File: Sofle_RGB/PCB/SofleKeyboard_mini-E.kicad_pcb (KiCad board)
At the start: 2 copper layers, 143.4 x 111.8 mm, 97 parts, among them J1 LED, J2 4PIN, J3 OLED, J4 key leds, J5 backlight sel, J6 indicator bypass, P1 i2c_pin, P2 i2c_pin, SW1 SW_PUSH-MX_W_LED, SW10 SW_PUSH-MX_W_LED, SW11 SW_PUSH-MX_W_LED, SW12 SW_PUSH-MX_W_LED, SW13 SW_PUSH-MX_W_LED, SW14 SW_PUSH-MX_W_LED, SW15 SW_PUSH-MX_W_LED, SW16 SW_PUSH-MX_W_LED, SW17 SW_PUSH-MX_W_LED, SW18 SW_PUSH-MX_W_LED, SW19 SW_PUSH-MX_W_LED, SW2 SW_PUSH-MX_W_LED, SW20 SW_PUSH-MX_W_LED, SW21 SW_PUSH-MX_W_LED, SW22 SW_PUSH-MX_W_LED, SW23 SW_PUSH-MX_W_LED, SW24 SW_PUSH-MX_W_LED, SW25 Rotary_Encoder_Switch, SW26 SW_PUSH-MX_W_LED, SW27 SW_PUSH-MX_W_LED, SW28 SW_PUSH-MX_W_LED, SW29 SW_PUSH-MX_W_LED, SW3 SW_PUSH-MX_W_LED, SW30 SW_PUSH-MX_W_LED, SW4 SW_PUSH-MX_W_LED, SW5 SW_PUSH-MX_W_LED, SW6 SW_PUSH-MX_W_LED, SW7 SW_PUSH-MX_W_LED, SW8 SW_PUSH-MX_W_LED, SW9 SW_PUSH-MX_W_LED, U1 ProMicro

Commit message: SK6812 mini-e RGB
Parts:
- D31, D32, D33, D34, D35, D36, D37: value LED_sk2812_SM -> LED-SK6812MINI-E; footprint LED_SMD:SK6812MINI_underglow_dev -> SofleRGB:SK6812MINI-E(mini_pinout)
- moved D34 7.95 mm to (106.7, 131.8), turned to 180 degrees
- moved D37 6.37 mm to (99.4, 86.5), turned to 90 degrees
- moved D33 5.57 mm to (196.6, 66.8)
- moved D35 5.45 mm to (149.0, 123.7), turned to 180 degrees
- moved D32 5.43 mm to (158.6, 59.2), turned to 180 degrees
- moved D31 4.91 mm to (120.5, 64.4)
- moved D36 4.16 mm to (187.3, 123.8), turned to 180 degrees
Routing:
- net Net-(SW22-Pad3): track 0.00 -> 74.4 mm, vias 0 -> 3
- net Net-(SW20-Pad3): track 1.18 -> 74.0 mm, vias 0 -> 6
- net Net-(SW24-Pad3): track 11.2 -> 82.2 mm, vias 1 -> 4
- net Net-(SW21-Pad1): track 0.00 -> 65.1 mm, vias 0 -> 2
- net Net-(SW23-Pad1): track 0.00 -> 47.8 mm, vias 0 -> 4
- net Net-(SW13-Pad3): track 0.00 -> 36.6 mm, vias 1 -> 3
- net Net-(SW11-Pad3): track 0.00 -> 35.1 mm, vias 0 -> 3
- net Net-(SW11-Pad1): track 0.00 -> 34.8 mm, vias 0 -> 3
- net Net-(SW13-Pad1): track 1.19 -> 35.8 mm, vias 0 -> 3
- net Net-(SW12-Pad1): track 0.00 -> 33.8 mm, vias 0 -> 2
- net Net-(SW12-Pad3): track 0.00 -> 33.3 mm, vias 0 -> 3
- net Net-(SW1-Pad1): track 0.00 -> 33.2 mm, vias 0 -> 2
- net Net-(SW3-Pad1): track 0.00 -> 32.3 mm, vias 0 -> 2
- net Net-(SW15-Pad1): track 0.00 -> 31.5 mm, vias 0 -> 3
- net Net-(SW2-Pad3): track 0.00 -> 31.1 mm, vias 0 -> 2
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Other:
- outline, holes or cut-outs redrawn

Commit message: Address PR comments + extra cleanup
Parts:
- SW1, SW10, SW11, SW12, SW13, SW14, SW15, SW16, SW17, SW18, SW19, SW2, SW20, SW21, SW22, SW23, SW24, SW26, SW27, SW28, SW29, SW3, SW30, SW4, SW5, SW6, SW7, SW8, SW9: footprint Dane:SK6812MINI-E_and_cherry(mini_pinout) -> SofleRGB:SK6812MINI-E_and_cherry(mini_pinout)
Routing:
- net GND: track 1077.0 -> 1079.7 mm, vias 246 -> 249
- net Net-(SW15-Pad1): track 31.5 -> 33.0 mm
- net Net-(SW14-Pad1): track 31.7 -> 30.4 mm
- net row3: track 190.7 -> 192.0 mm
- net Net-(SW21-Pad1): track 65.1 -> 64.0 mm
- net Net-(SW16-Pad3): track 30.7 -> 31.7 mm
- net Net-(SW22-Pad3): track 74.4 -> 73.4 mm
- net Net-(SW23-Pad1): track 47.8 -> 47.0 mm
- net Net-(SW14-Pad3): track 29.7 -> 28.9 mm
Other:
- board text added: "Sofle RGB v3.0, Dane Evans, Gustavo Baratto"
- board text removed: "&BL"
- board text removed: "Sofle RGB v2.0, Dane Evans"

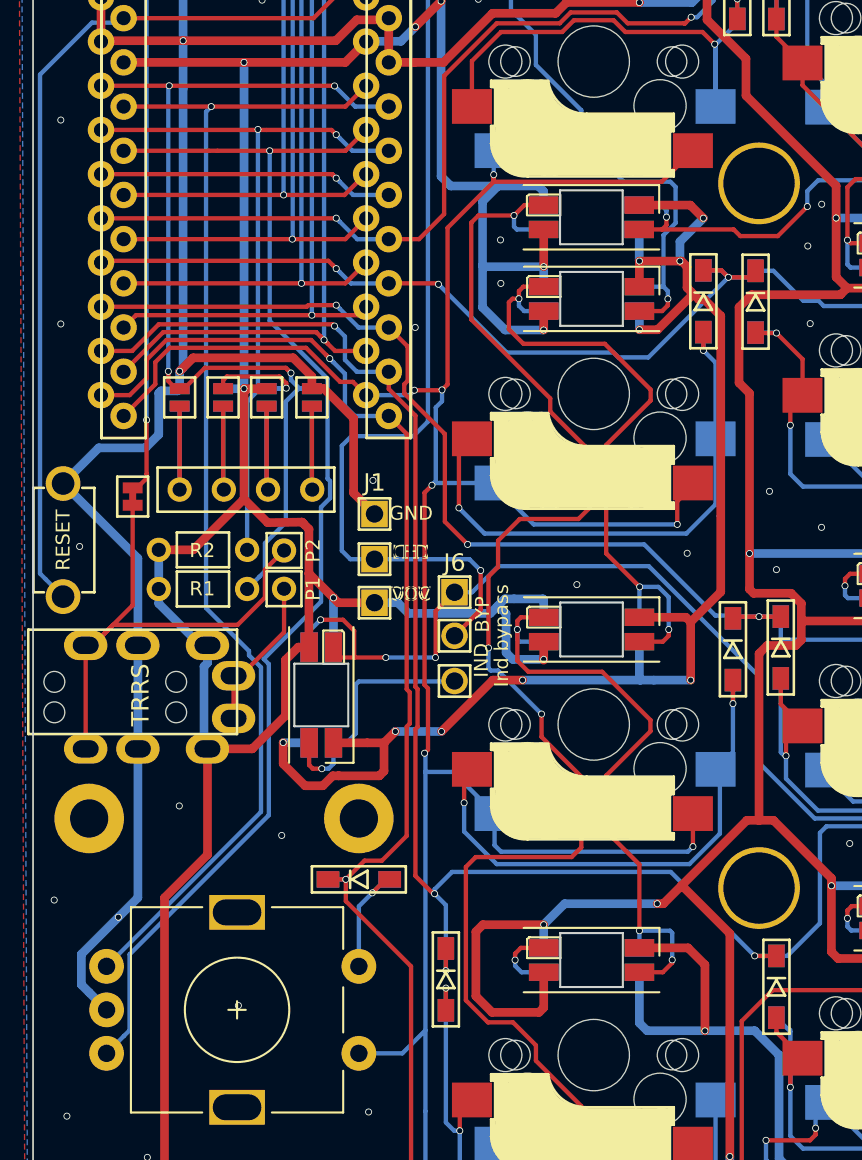
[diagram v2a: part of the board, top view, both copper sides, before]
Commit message: Remove extra silk in J1 + tidy up a few more traces
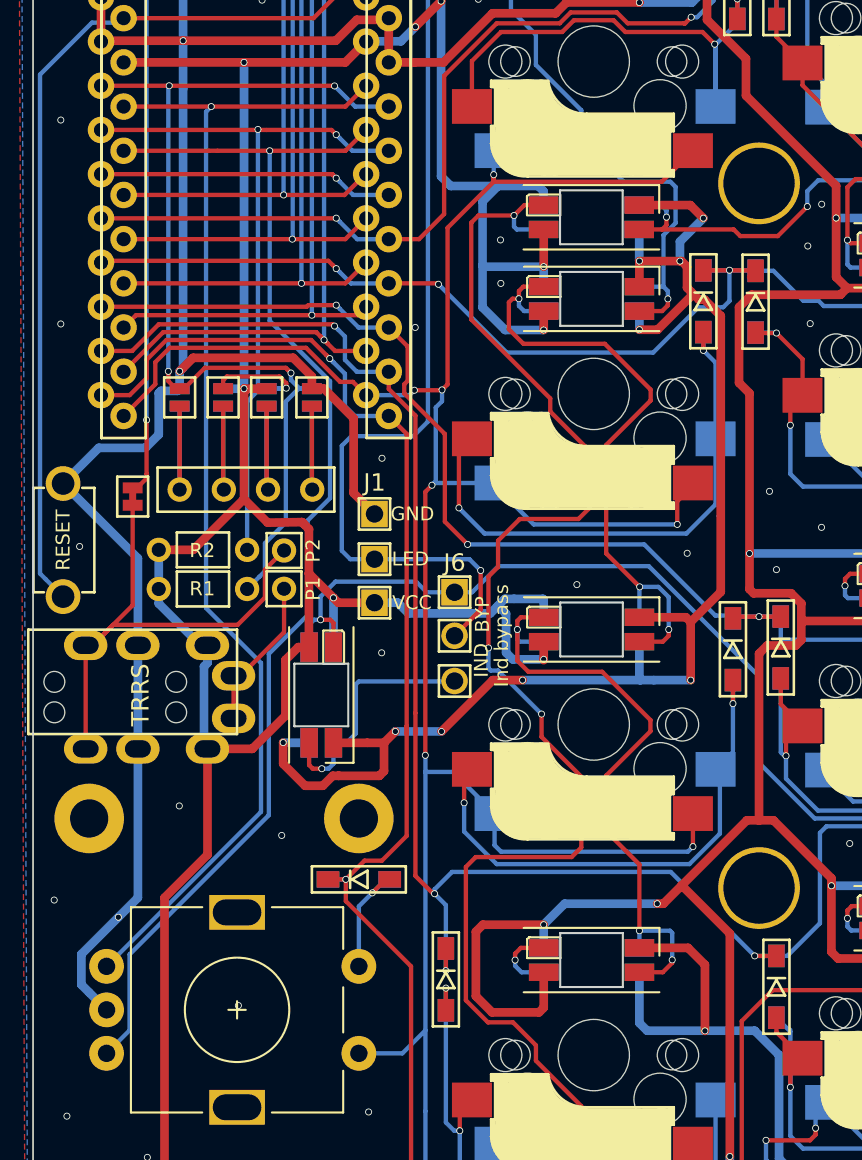
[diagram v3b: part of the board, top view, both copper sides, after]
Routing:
- net lights: track 102.4 -> 101.0 mm, vias 5 -> 3
- net row1: track 144.1 -> 145.2 mm
- net GND: vias 249 -> 250
